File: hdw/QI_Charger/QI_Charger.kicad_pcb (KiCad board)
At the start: 4 copper layers, 150 x 50 mm, 303 parts, among them J1001 USB_B_Mini, J1301 PAD, J1302 PAD, J201 +12V IN, J401 PICKIT3, Q201 IPC100N04S51R7ATMA1, Q202 IPC100N04S51R7ATMA1, Q401 BSS214NW, SW401 MRST, SW801 Cap_Touch, SW802 Cap_Touch, U1001 LT6700-1-S6, U1002 FT234XD, U1003 74LVC1G06, U1004 TPD3S014DBVR, U1101 74LVC1G06, U1102 74LVC1G07, U1103 74LVC1G07, U1104 74LVC1G06, U1105 74LVC1G07, U1106 74LVC1G06, U1107 74LVC1G06, U1108 74LVC1G06, U1109 74LVC1G06, U1201 LM73-1, U1202 LM73-1, U1203 LM73-1, U1301 INA138, U1302 NXQ1TXH5_101J, U1401 74LVC1G14, U1402 74LVC1G14, U1403 74LVC1G17, U201 LTC4365DDB, U202 INA138, U301 TPS62130, U302 74LVC1G17, U501 74LVC1G17, U502 74LVC1G17, U503 PIC18F27K40T-I_ML, U601 OPA340NA, U602 OPA340NA, U603 OPA340NA, U604 OPA340NA, U701 SSD1306, U801 AT42QT1010-TSHR, U802 AT42QT1010-TSHR, U901 ISO7321C, Y1301 32.768kHz

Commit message: Started routing
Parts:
- C205, C206, C207: moved to F.Cu
- C208, R210, U202: moved to B.Cu
- moved C1304 13.1 mm to (172.6, 53.8), turned to 0 degrees
- moved C1302 11.2 mm to (172.6, 55.2), turned to 0 degrees
- moved C1306 9.46 mm to (177.0, 60.5), turned to 270 degrees
- moved C1301 9.29 mm to (172.6, 56.6), turned to 0 degrees
- moved R1304 7.49 mm to (175.5, 60.5), turned to 270 degrees
- moved C208 6.56 mm to (67.8, 70.2), turned to 0 degrees
- moved R210 4.41 mm to (67.8, 68.7), turned to 0 degrees
- moved U1301 3.56 mm to (172.6, 61.2), turned to 180 degrees
- moved C205 2.26 mm to (67.8, 67.2), turned to 180 degrees
- moved C207 1.73 mm to (67.8, 64.4), turned to 180 degrees
- moved C1201 1.63 mm to (169.8, 69.8)
- moved R1201 1.63 mm to (163.4, 68.2)
- moved R1202 1.63 mm to (163.4, 69.7)
- moved R1207 1.63 mm to (163.4, 71.2), turned to 0 degrees
- moved R1210 1.63 mm to (163.4, 66.7), turned to 0 degrees
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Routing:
- net +5V: track 0.00 -> 74.6 mm, vias 0 -> 27
- net GND: track 0.00 -> 67.7 mm, vias 0 -> 90
- net +12Vin: track 0.00 -> 43.8 mm
- net Net-(C1322-Pad1): track 0.00 -> 26.3 mm
- net Net-(C1317-Pad1): track 0.00 -> 25.9 mm
- net Net-(Q202-Pad5): track 0.00 -> 25.8 mm, vias 0 -> 1
- net QI_NTC: track 0.00 -> 20.0 mm, vias 0 -> 2
- net Net-(C1303-Pad1): track 0.00 -> 18.3 mm
- net +12V: track 0.00 -> 18.3 mm, vias 0 -> 1
- net Net-(C1318-Pad1): track 0.00 -> 10.2 mm
- net Net-(R1302-Pad2): track 0.00 -> 8.30 mm
- net Net-(C801-Pad2): track 0.00 -> 7.12 mm
- net Net-(C802-Pad2): track 0.00 -> 7.12 mm
- net POS12_PGOOD: track 0.00 -> 7.08 mm
- net POS12_ISNS_ADC: track 0.00 -> 7.03 mm
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- added copper zone on F.Cu, net +12V
- added copper zone on F.Cu, net +12Vin
- added copper zone on PWR, net +5V
- added copper zone on PWR, net +5V_USB
- added copper zone on GND, net GND
- added copper zone on GND, net GND_USB
- added copper zone on F.Cu, net Net-(Q201-Pad1)
- added copper zone on F.Cu, net Net-(Q202-Pad5)

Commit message: More routing
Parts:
- moved R1208 4.57 mm to (81.7, 56.0), turned to 270 degrees
- moved R1211 4.57 mm to (86.2, 56.0), turned to 270 degrees
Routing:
- net +5V: track 74.6 -> 104.2 mm, vias 27 -> 52
- net Net-(R205-Pad1): track 4.00 -> 29.1 mm, vias 0 -> 3
- net GND: track 67.7 -> 87.2 mm, vias 90 -> 98
- net +12V: track 18.3 -> 25.9 mm
- net Net-(R302-Pad2): track 0.00 -> 6.66 mm
- net POS5_PGOOD: track 0.00 -> 4.65 mm
- net Net-(R306-Pad2): track 0.00 -> 3.40 mm
- net /Temperature Sensors/Temp2_I2C_SCL: track 0.00 -> 3.36 mm
- net /Temperature Sensors/Temp2_I2C_SDA: track 0.00 -> 3.26 mm
- net Net-(C302-Pad1): track 0.00 -> 3.09 mm
- added copper zone on F.Cu, net +5V
- added copper zone on F.Cu, net GND
- added copper zone on F.Cu, net Net-(L301-Pad1)

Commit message: More routing
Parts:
- moved C1315 3.00 mm to (174.8, 72.6), turned to 0 degrees
- moved C1313 3.00 mm to (174.8, 71.1), turned to 0 degrees
- moved R1313 2.62 mm to (172.0, 72.6), turned to 0 degrees
- moved R1312 2.62 mm to (172.0, 71.1), turned to 0 degrees
- moved C1002 1.46 mm to (66.0, 85.3)
- moved C601 1.40 mm to (74.4, 72.4)
- moved C603 1.40 mm to (74.4, 73.8)
- moved U601 1.40 mm to (74.4, 73.8)
- moved C605 1.40 mm to (74.4, 75.2)
- moved C1004 1.02 mm to (66.9, 77.0)
- moved C1006 1.02 mm to (66.9, 75.1)
- moved U1004 0.97 mm to (54.8, 76.6)
- moved C1008 0.72 mm to (53.7, 80.1)
- moved L1001 0.51 mm to (48.8, 77.3)
- moved C1011 0.51 mm to (50.6, 77.3)
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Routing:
- net +5V: track 104.2 -> 164.3 mm, vias 52 -> 76
- net GND: track 87.2 -> 144.5 mm, vias 98 -> 126
- net +5V_USB: track 0.00 -> 33.3 mm, vias 0 -> 22
- net +12V: track 25.9 -> 57.6 mm
- net GND_USB: track 0.00 -> 27.5 mm, vias 0 -> 36
- net /USB UART Bridge/CONN_USB+: track 0.00 -> 24.4 mm, vias 0 -> 1
- net Net-(J1001-Pad6): track 0.00 -> 23.2 mm
- net /USB UART Bridge/CONN_USB-: track 0.00 -> 23.2 mm, vias 0 -> 1
- net ~USB_ACTIVE: track 0.00 -> 16.0 mm, vias 0 -> 1
- net Net-(D1001-Pad1): track 0.00 -> 15.8 mm, vias 0 -> 2
- net USB_UART_TX_ISO: track 0.00 -> 12.3 mm, vias 0 -> 2
- net /USB UART Bridge/POS5_USB_PGOOD: track 0.00 -> 11.1 mm, vias 0 -> 2
- net POS12_ISNS: track 3.64 -> 13.7 mm, vias 0 -> 1
- net Net-(C1011-Pad1): track 0.00 -> 9.00 mm
- net USB_UART_RX_ISO: track 0.00 -> 8.27 mm, vias 0 -> 2
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- added copper zone on F.Cu, net +5V_USB
- added copper zone on F.Cu, net GND_USB

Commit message: Finished routing
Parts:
- moved R501 1.27 mm to (131.3, 55.1)
- moved R502 1.27 mm to (129.8, 55.1)
- moved R503 1.27 mm to (128.3, 55.1)
- moved R504 1.27 mm to (132.8, 55.1)
- moved R603 1.09 mm to (120.8, 56.2), turned to 270 degrees
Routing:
- net I2C_SCL: track 0.00 -> 122.6 mm, vias 0 -> 3
- net I2C_SDA: track 0.00 -> 115.2 mm, vias 0 -> 4
- net QI_LED_G: track 4.84 -> 74.3 mm, vias 2 -> 5
- net Net-(R603-Pad2): track 0.00 -> 63.7 mm, vias 0 -> 2
- net GND: track 144.5 -> 205.7 mm, vias 126 -> 151
- net USB_UART_TX: track 2.38 -> 61.3 mm, vias 1 -> 3
- net USB_UART_RX: track 2.26 -> 61.0 mm, vias 1 -> 3
- net QI_Standby: track 4.82 -> 63.2 mm, vias 0 -> 2
- net ~ACTIVE_LED: track 3.04 -> 55.1 mm, vias 1 -> 2
- net POS5_SW_SNS: track 0.00 -> 51.6 mm, vias 0 -> 3
- net QI_LED_R: track 5.04 -> 55.6 mm, vias 2 -> 3
- net QI_SW_SNS: track 1.71 -> 48.9 mm, vias 0 -> 2
- net +5V: track 164.3 -> 211.3 mm, vias 76 -> 104
- net Net-(R605-Pad2): track 3.33 -> 44.4 mm, vias 0 -> 1
- net I2C_Error_LED: track 3.04 -> 43.2 mm, vias 1 -> 2
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- added copper zone on F.Cu, net +5VP
- added copper zone on PWR, net +5VP
- added copper zone on F.Cu, net Net-(C1314-Pad1)
- added copper zone on F.Cu, net Net-(C1314-Pad2)
- added copper zone on F.Cu, net QI_SW

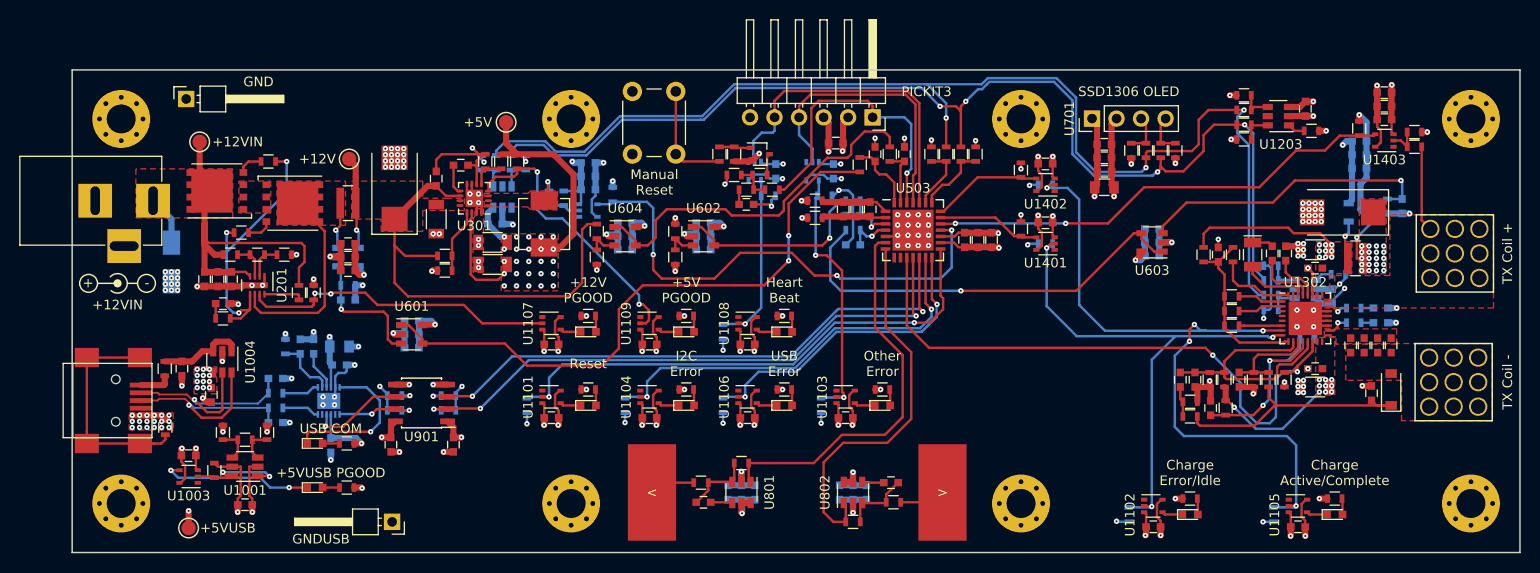
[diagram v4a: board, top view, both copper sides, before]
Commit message: Added communications test points
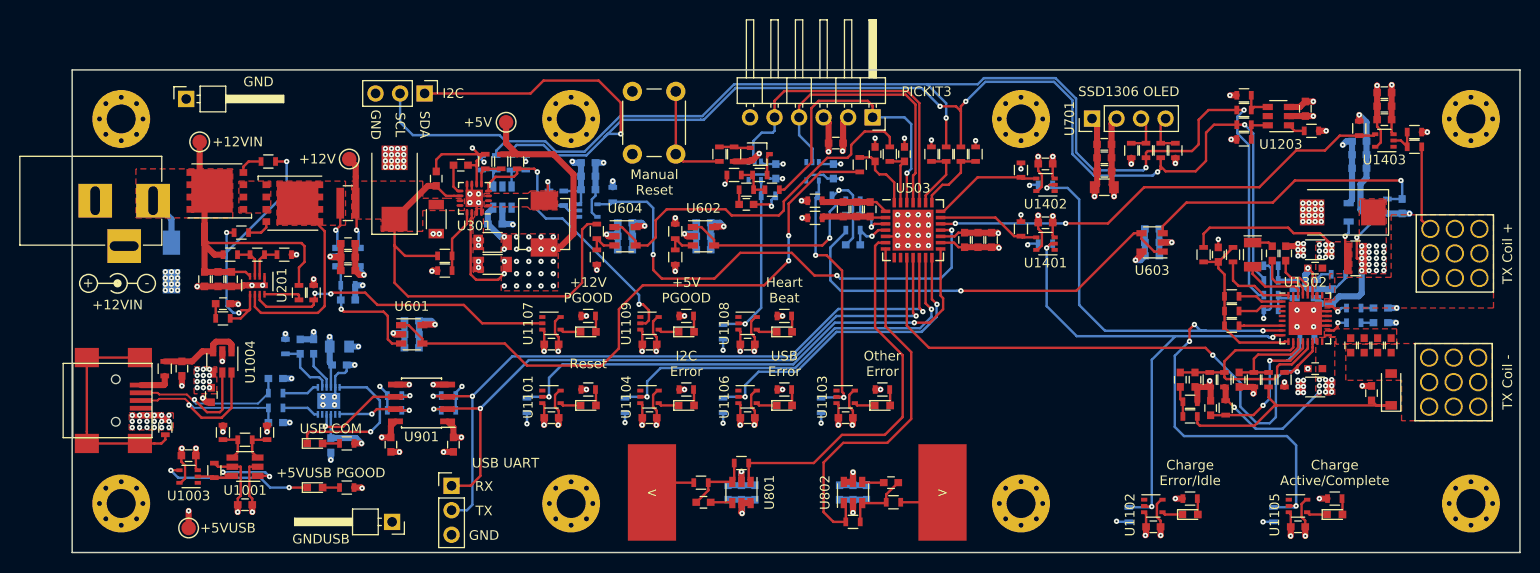
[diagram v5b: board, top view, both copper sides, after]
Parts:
- added J701: I2C, Pin_Headers:Pin_Header_Straight_1x03_Pitch2.54mm, F.Cu at (75.8, 48.8)
- added J901: UART, Pin_Headers:Pin_Header_Straight_1x03_Pitch2.54mm, F.Cu at (78.5, 89.5)
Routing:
- net I2C_SDA: track 115.2 -> 142.8 mm, vias 4 -> 5
- net I2C_SCL: track 122.6 -> 137.1 mm
- net USB_UART_TX: track 61.3 -> 74.9 mm
- net USB_UART_RX: track 61.0 -> 71.4 mm
- net +5V: track 211.3 -> 215.1 mm, vias 104 -> 103
- net GND: track 205.7 -> 208.9 mm, vias 151 -> 150
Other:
- board text added: "I2C"
- board text added: "RX"
- board text added: "SCL"
- board text added: "SDA"
- board text added: "TX"
- board text added: "USB UART"

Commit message: Added a bunch of graphical items to PCB
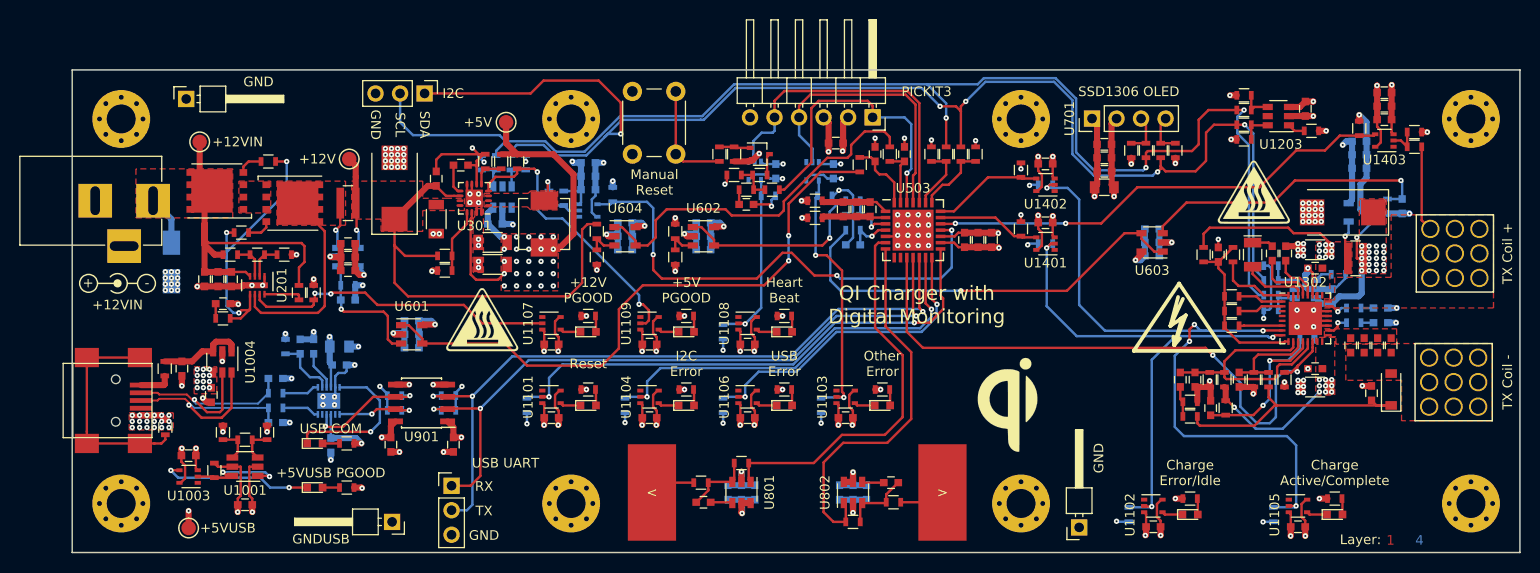
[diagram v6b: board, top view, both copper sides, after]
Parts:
- added G***: Heat_Caution_Symbol, Custom Footprints Library:Heat_Caution_Symbol, F.Cu at (161.7, 59.1)
- added G***: NXP_Logo, Custom Footprints Library:NXP_Logo, B.Cu at (158.9, 83.9)
- added G***: Texas_Instruments_Logo, Custom Footprints Library:Texas_Instruments_Logo, B.Cu at (160.8, 51.6)
- added G***: Visahy_Logo, Custom Footprints Library:Visahy_Logo, B.Cu at (160.8, 59.9)
- added G***: Wurth_Logo, Custom Footprints Library:Wurth_Logo, B.Cu at (150.7, 70.7)
- added G***: RoHS_Compliance_Logo, Custom Footprints Library:RoHS_Compliance_Logo, B.Cu at (61.0, 56.6)
- added G***: Heat_Caution_Symbol, Custom Footprints Library:Heat_Caution_Symbol, F.Cu at (81.7, 72.3)
- added G***: QI_Logo, Custom Footprints Library:QI_Logo, F.Cu at (136.1, 81.1)
- added G***: QI_Logo_Massive, Custom Footprints Library:QI_Logo_Massive, B.Cu at (106.4, 72.4)
- added G***: Infineon_Logo, Custom Footprints Library:Infineon_Logo, B.Cu at (171.9, 77.5)
- added G***: Kemet_Logo, Custom Footprints Library:Kemet_Logo, B.Cu at (171.9, 84.7)
- added G***: LTC_Logo, Custom Footprints Library:LTC_Logo, B.Cu at (145.7, 77.2)
- added G***: Microchip_Logo, Custom Footprints Library:Microchip_Logo, B.Cu at (145.7, 84.3)
- added G***: Murata_Logo, Custom Footprints Library:Murata_Logo, B.Cu at (158.9, 77.3)
- added REF**: Symbol_HighVoltage_Type2_Silkscreen_VerySmall, Custom Footprints Library:Symbol_HighVoltage_Type2_Silkscreen_VerySmall, F.Cu at (153.9, 72.7)
- added TP204: TP, Pin_Headers:Pin_Header_Angled_1x01_Pitch2.54mm, F.Cu at (143.6, 93.8)
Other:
- board text added: "1"
- board text added: "1/15/2019"
- board text added: "2"
- board text added: "3"
- board text added: "4"
- board text added: "Layer:"
- board text added: "QI Charger with Digital Monitoring"

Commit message: BOM changes, gitignore
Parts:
- added G***: Owl_1_Logo, Custom Footprints Library:Owl_1_Logo, B.Cu at (47.8, 76.1)
- U1103: value 74LVC1G07 -> 74LVC1G06
